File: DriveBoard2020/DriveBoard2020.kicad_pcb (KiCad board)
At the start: 2 copper layers, 57 parts, among them SW0 SW_SPST, SW1 SW_Push, SW2 SW_Push, SW3 SW_Push, SW4 SW_Push, SW5 SW_Push, SW6 SW_Push, U1 MAX232, U2 MAX232, U3 OKI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

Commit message: worked really hard on making layout pretty
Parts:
- moved C6 4.10 mm to (92.3, 49.5)
- moved Conn1 0.13 mm to (105.3, 70.4)
- turned C2 to 270 degrees
- turned C7 to 270 degrees
- turned D10 to 270 degrees
- turned D11 to 270 degrees
- turned D12 to 270 degrees
- turned D13 to 270 degrees
- turned D14 to 270 degrees
- turned D6 to 90 degrees
- turned D8 to 270 degrees
- turned D9 to 270 degrees
- turned R10 to 270 degrees
- turned R12 to 270 degrees
- turned R13 to 270 degrees
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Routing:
- net Tx3: track 158.1 -> 62.5 mm
- net GND: track 94.3 -> 0.00 mm, vias 6 -> 0
- net Tx4: track 111.0 -> 158.3 mm, vias 3 -> 4
- net FR_Motor: track 46.7 -> 10.6 mm, vias 1 -> 0
- net MR_Motor: track 45.5 -> 10.6 mm, vias 1 -> 0
- net +5V: track 90.5 -> 56.2 mm
- net ML_Motor: track 32.8 -> 10.6 mm, vias 1 -> 0
- net switch_direction: track 21.0 -> 0.00 mm, vias 2 -> 0
- net Rx4: track 75.3 -> 88.8 mm, vias 2 -> 4
- net R5_In: track 12.4 -> 0.00 mm
- net Rx6: track 80.1 -> 91.5 mm, vias 2 -> 4
- net Rx3: track 102.1 -> 90.9 mm, vias 0 -> 1
- net RL_Motor: track 40.0 -> 48.7 mm
- net RR_Motor: track 45.4 -> 53.6 mm, vias 1 -> 2
- net R4_In: track 27.6 -> 35.1 mm
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
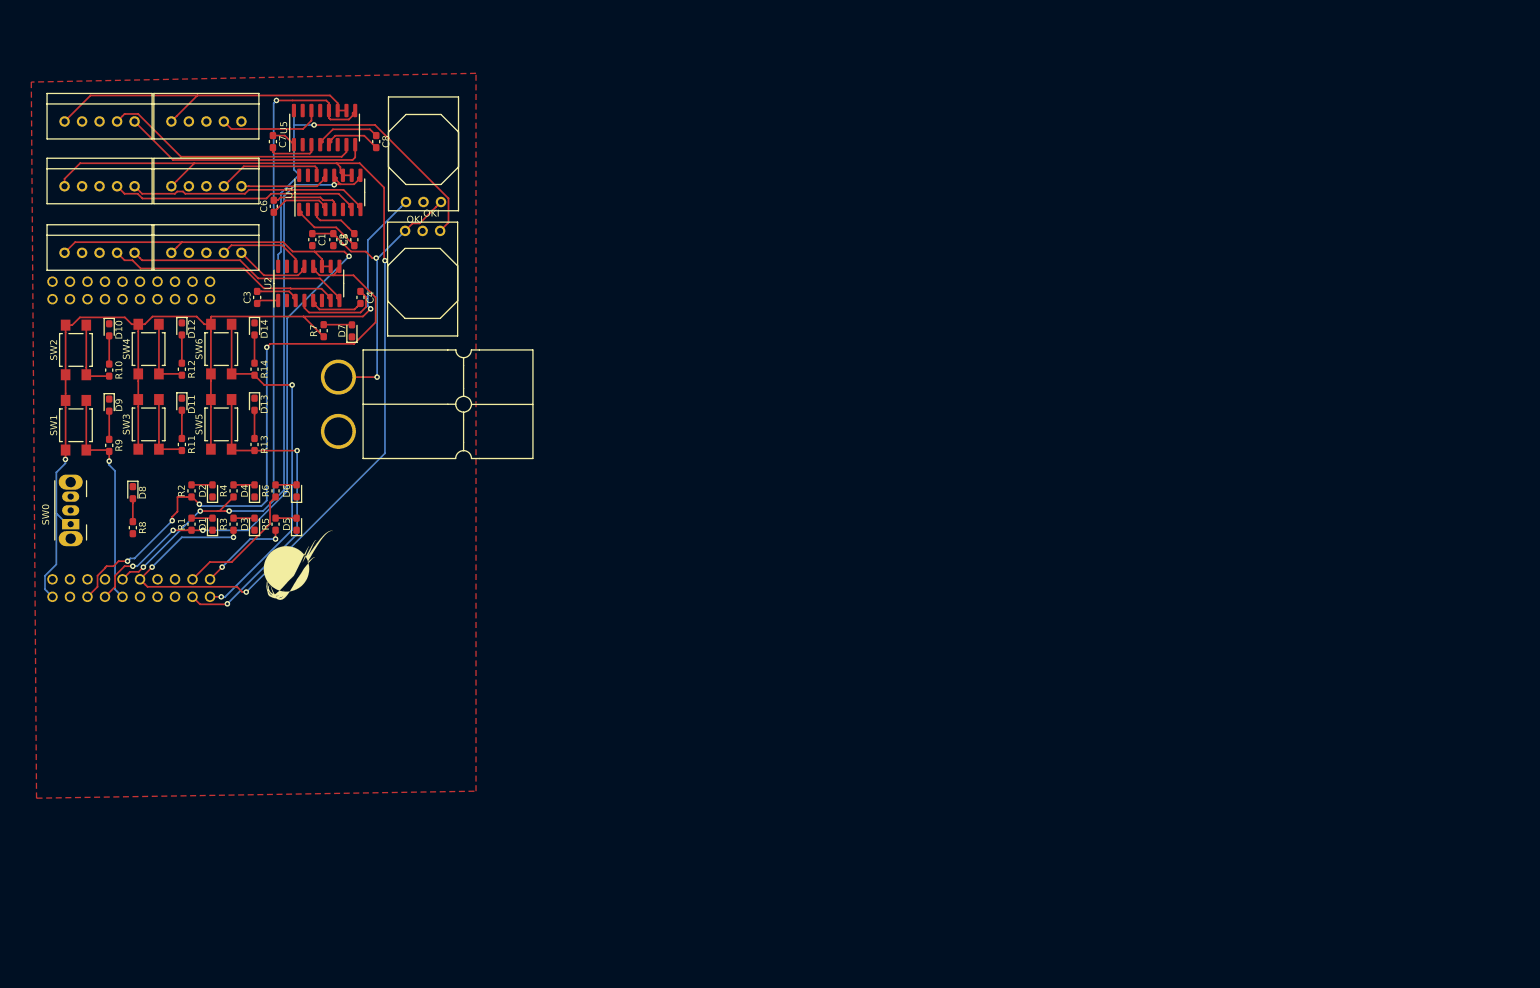
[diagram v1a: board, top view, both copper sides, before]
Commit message: changed and wired 3232's
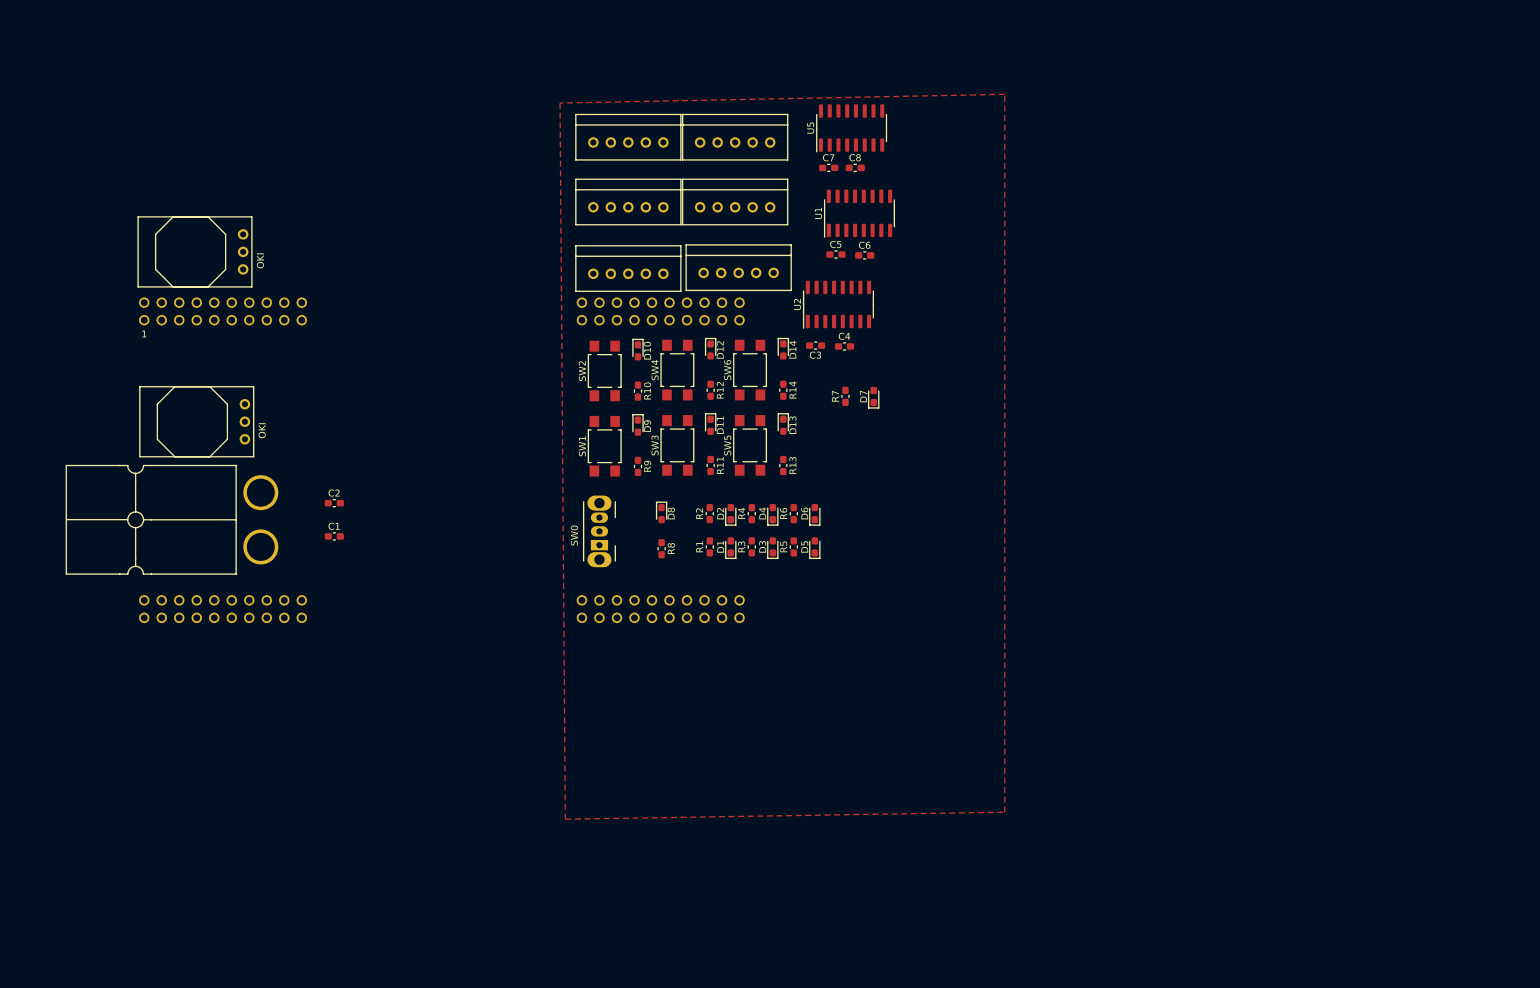
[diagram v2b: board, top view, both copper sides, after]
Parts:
- removed G***: LOGO, MRDT_Silkscreens:0_MRDT_Logo_10mm
- U1, U2, U5: value MAX232 -> MAX_3232
- U4: footprint MRDT_Shields:TM4C129E_Launchpad_X7_THT_BOTTOM -> MRDT_Shields:TM4C129E_Launchpad_FULL_THT_BOTTOM
- moved C6 86.0 mm to (178.1, 56.6), turned to 0 degrees
- moved C3 81.3 mm to (170.9, 69.7), turned to 180 degrees
- moved C7 80.7 mm to (172.8, 43.9), turned to 0 degrees
- moved Conn2 77.3 mm to (159.8, 59.2)
- moved U1 76.9 mm to (177.3, 50.5)
- moved U2 76.9 mm to (174.2, 63.8)
- moved Conn3 76.8 mm to (159.3, 49.7)
- moved Conn4 76.8 mm to (159.3, 40.3)
- moved Conn5 76.8 mm to (143.8, 59.3)
- moved Conn6 76.8 mm to (143.8, 49.7)
- moved Conn7 76.8 mm to (143.8, 40.3)
- moved D10 76.8 mm to (145.2, 70.5)
- moved D11 76.8 mm to (155.7, 81.3)
- moved D12 76.8 mm to (155.7, 70.4)
- moved D13 76.8 mm to (166.2, 81.3)
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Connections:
- Conn3 pad 4: T3_Out -> T2_Out
- Conn3 pad 5: R3_In -> R2_In
- Conn4 pad 4: T5_Out -> T3_Out
- Conn4 pad 5: R5_In -> R3_In
- Conn5 pad 4: T2_Out -> T1_Out
- Conn5 pad 5: R2_In -> R1_In
- Conn6 pad 4: T4_Out -> T2_Out
- Conn6 pad 5: R4_In -> R2_In
- Conn7 pad 4: T6_Out -> T3_Out
- Conn7 pad 5: R6_In -> R3_In
- U1 pad 10: Tx4 -> Net-(U1-Pad10)
- U1 pad 13: R3_In -> R2_In
- U1 pad 14: T3_Out -> T2_Out
- U1 pad 7: T4_Out -> Net-(U1-Pad7)
- U1 pad 8: R4_In -> Net-(U1-Pad8)
- U1 pad 9: Rx4 -> Net-(U1-Pad9)
- U2 pad 1: Net-(C3-Pad1) -> Net-(C3-Pad2)
- U2 pad 10: Tx6 -> Net-(U2-Pad10)
- U2 pad 3: Net-(C3-Pad2) -> Net-(C3-Pad1)
- U2 pad 7: T2_Out -> Net-(U2-Pad7)
- U2 pad 8: R2_In -> Net-(U2-Pad8)
- U2 pad 9: Rx6 -> Net-(U2-Pad9)
- U5 pad 10: Tx3 -> Net-(U5-Pad10)
- U5 pad 13: R5_In -> R3_In
- U5 pad 14: T5_Out -> T3_Out
- U5 pad 7: T6_Out -> Net-(U5-Pad7)
- U5 pad 8: R6_In -> Net-(U5-Pad8)
- U5 pad 9: Rx3 -> Net-(U5-Pad9)
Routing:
- net Tx4: track 158.3 -> 0.00 mm, vias 4 -> 0
- net +3V3: track 149.8 -> 0.00 mm, vias 2 -> 0
- net Tx6: track 120.3 -> 0.00 mm, vias 4 -> 0
- net Rx6: track 91.5 -> 0.00 mm, vias 4 -> 0
- net Rx3: track 90.9 -> 0.00 mm, vias 1 -> 0
- net Rx4: track 88.8 -> 0.00 mm, vias 4 -> 0
- net Tx3: track 62.5 -> 0.00 mm, vias 2 -> 0
- net +5V: track 56.2 -> 0.00 mm, vias 1 -> 0
- net RR_Motor: track 53.6 -> 0.00 mm, vias 2 -> 0
- net RL_Motor: track 48.7 -> 0.00 mm, vias 2 -> 0
- net +12V: track 46.4 -> 0.00 mm, vias 2 -> 0
- net T6_Out: track 37.6 -> 0.00 mm
- net R6_In: track 36.3 -> 0.00 mm
- net T4_Out: track 36.2 -> 0.00 mm
- net R4_In: track 35.1 -> 0.00 mm
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
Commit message: created netlist, began layout
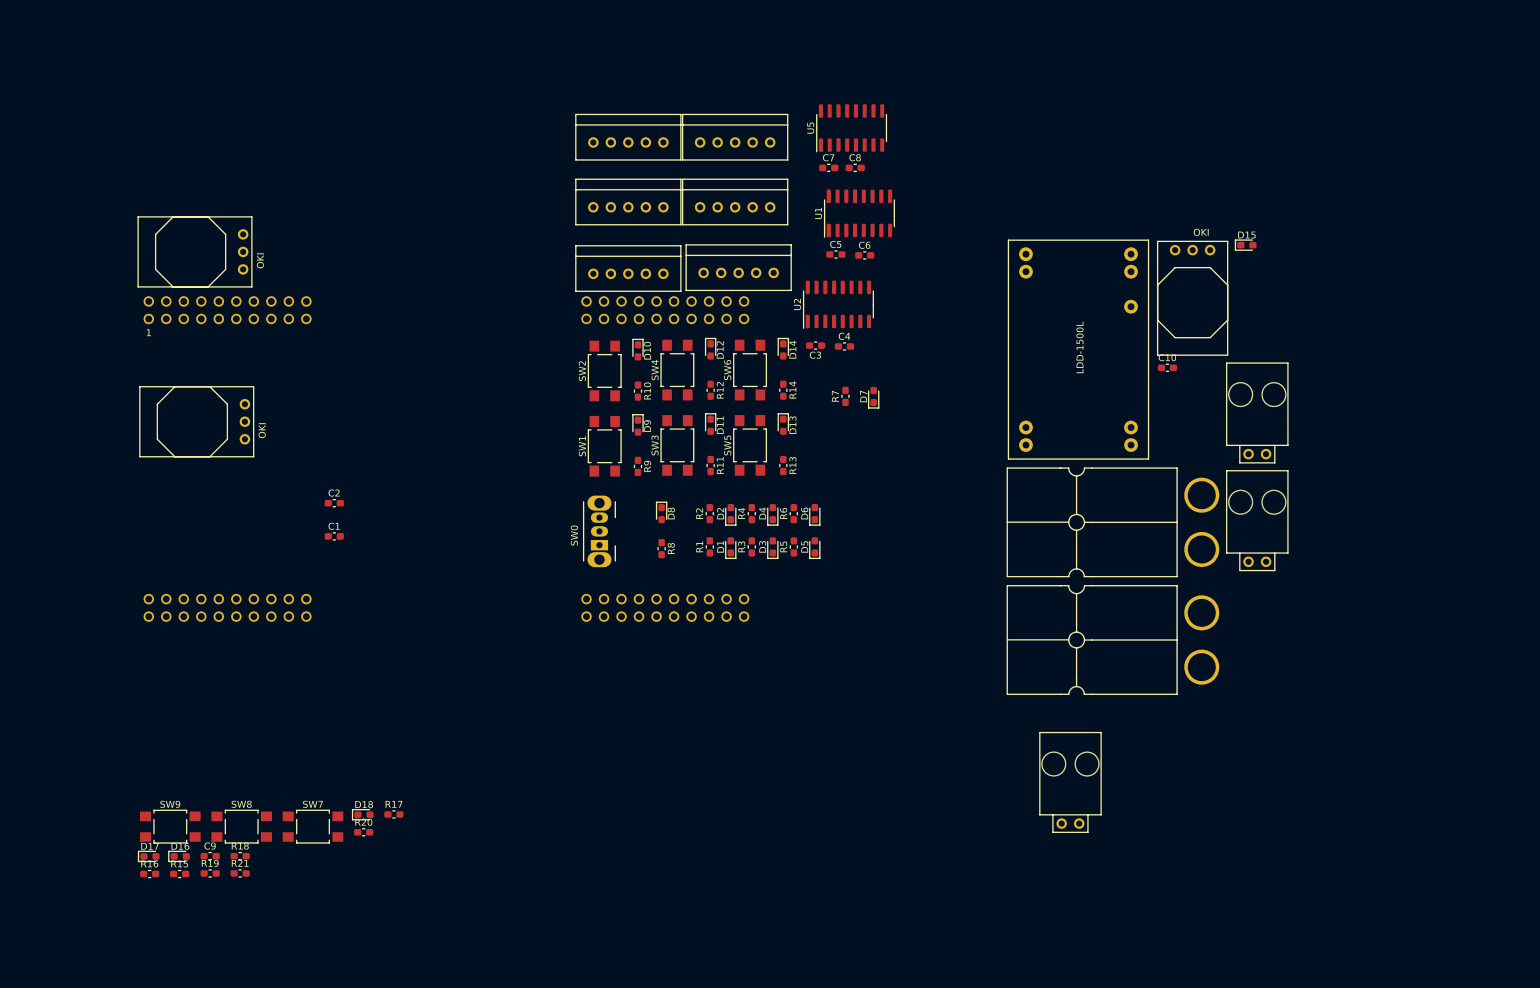
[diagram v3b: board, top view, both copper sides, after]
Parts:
- added C10: 10uF, Capacitor_SMD:C_0603_1608Metric_Pad1.05x0.95mm_HandSolder, F.Cu at (222.0, 72.9)
- added C9: 10uF, Capacitor_SMD:C_0603_1608Metric_Pad1.05x0.95mm_HandSolder, F.Cu at (83.1, 143.8)
- added Conn10: Molex_SL_02, MRDT_Connectors:MOLEX_SL_02_Horizontal, F.Cu at (207.9, 139.1)
- added Conn11: Molex_SL_02, MRDT_Connectors:MOLEX_SL_02_Horizontal, F.Cu at (235.0, 101.1)
- added Conn8: AndersonPP, MRDT_Connectors:Anderson_2_Horizontal_Side_by_Side, F.Cu at (223.4, 120.3)
- added Conn9: Molex_SL_02, MRDT_Connectors:MOLEX_SL_02_Horizontal, F.Cu at (235.0, 85.5)
- added D15: G_LED, LED_SMD:LED_0603_1608Metric_Pad1.05x0.95mm_HandSolder, F.Cu at (233.5, 55.2)
- added D16: G_LED, LED_SMD:LED_0603_1608Metric_Pad1.05x0.95mm_HandSolder, F.Cu at (78.8, 143.8)
- added D17: Org_LED, LED_SMD:LED_0603_1608Metric_Pad1.05x0.95mm_HandSolder, F.Cu at (74.4, 143.8)
- added D18: Org_LED, LED_SMD:LED_0603_1608Metric_Pad1.05x0.95mm_HandSolder, F.Cu at (105.4, 137.8)
- added R15: 10K, Resistor_SMD:R_0603_1608Metric_Pad1.05x0.95mm_HandSolder, F.Cu at (78.7, 146.4)
- added R16: 10K, Resistor_SMD:R_0603_1608Metric_Pad1.05x0.95mm_HandSolder, F.Cu at (74.3, 146.4)
- added R17: 10K, Resistor_SMD:R_0603_1608Metric_Pad1.05x0.95mm_HandSolder, F.Cu at (109.8, 137.7)
- added R18: 500, Resistor_SMD:R_0603_1608Metric_Pad1.05x0.95mm_HandSolder, F.Cu at (87.4, 143.8)
- added R19: 500, Resistor_SMD:R_0603_1608Metric_Pad1.05x0.95mm_HandSolder, F.Cu at (83.1, 146.3)
- added R20: 500, Resistor_SMD:R_0603_1608Metric_Pad1.05x0.95mm_HandSolder, F.Cu at (105.4, 140.3)
- added R21: 500, Resistor_SMD:R_0603_1608Metric_Pad1.05x0.95mm_HandSolder, F.Cu at (87.4, 146.3)
- added SW7: SW_Push, Button_Switch_SMD:SW_SPST_TL3305A, F.Cu at (98.0, 139.5)
- added SW8: SW_Push, Button_Switch_SMD:SW_SPST_TL3305A, F.Cu at (87.7, 139.5)
- added SW9: SW_Push, Button_Switch_SMD:SW_SPST_TL3305A, F.Cu at (77.3, 139.5)
- added U7: OKI, MRDT_Devices:OKI_Horizontal, F.Cu at (220.5, 54.6)
- added U8: LDD-1500L, MRDT_Devices:LDD-1500L_LED_DRIVER, F.Cu at (198.9, 86.2)
- moved Conn1 136.5 mm to (223.4, 103.2)
- moved U4 0.68 mm to (72.9, 110.3)
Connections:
- U4 pad +3V3`: +3V3 -> (no net)
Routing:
- removed copper zone on F.Cu, net GND

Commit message: minor changes to layout
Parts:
- moved Conn8 136.9 mm to (87.6, 102.9)
- moved Conn1 136.7 mm to (87.6, 86.9)
- moved R14 116.8 mm to (267.0, 135.4)
- moved D14 116.8 mm to (267.0, 129.5)
- moved SW6 116.8 mm to (262.1, 132.5)
- moved D11 116.8 mm to (255.5, 141.9)
- moved D13 116.8 mm to (266.1, 141.9)
- moved R9 116.8 mm to (245.0, 147.8)
- moved SW1 116.8 mm to (240.2, 144.9)
- moved SW3 116.8 mm to (250.7, 144.8)
- moved D9 116.8 mm to (245.0, 142.0)
- moved R11 116.8 mm to (255.5, 147.7)
- moved R13 116.8 mm to (266.1, 147.7)
- moved SW5 116.8 mm to (261.2, 144.8)
- moved D10 116.1 mm to (245.2, 129.4)
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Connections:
- Conn8 pad 2: +12VA -> (no net)
- U4 pad PD4: FL_Motor -> Net-(U4-PadPD4)
- U4 pad PD5: FR_Motor -> Net-(U4-PadPD5)
- U4 pad PN4: RR_Motor -> Net-(U4-PadPN4)
- U4 pad PN5: RL_Motor -> Net-(U4-PadPN5)
- U4 pad PP4: MR_Motor -> Net-(U4-PadPP4)
- U4 pad PQ0: ML_Motor -> Net-(U4-PadPQ0)

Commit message: working on layout
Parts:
- moved D7 184.8 mm to (88.2, 44.6)
- moved R7 184.8 mm to (84.1, 44.6)
- moved D15 129.7 mm to (111.4, 98.9), turned to 90 degrees
- moved D9 129.6 mm to (136.3, 71.5)
- moved R9 129.6 mm to (136.3, 77.3)
- moved SW1 129.6 mm to (131.4, 74.4)
- moved D14 127.2 mm to (165.2, 53.1)
- moved R14 127.2 mm to (165.2, 59.0)
- moved SW6 127.2 mm to (160.4, 56.1)
- moved U7 127.1 mm to (99.6, 93.7)
- moved D13 126.3 mm to (175.9, 53.4)
- moved R13 126.3 mm to (175.9, 59.2)
- moved SW5 126.3 mm to (171.1, 56.3)
- moved D11 119.0 mm to (159.6, 71.5)
- moved SW3 119.0 mm to (154.7, 74.4)
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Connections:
- U4 pad +3V3: (no net) -> Net-(U4-Pad+3V3)
- U4 pad +5V: (no net) -> Net-(U4-Pad+5V)
- U4 pad PA6: (no net) -> Net-(U4-PadPA6)
- U4 pad PA7: (no net) -> Headlight_OnOff_PWM
- U4 pad PB2: (no net) -> Net-(U4-PadPB2)
- U4 pad PB3: (no net) -> Net-(U4-PadPB3)
- U4 pad PC4: (no net) -> Net-(U4-PadPC4)
- U4 pad PC5: (no net) -> Net-(U4-PadPC5)
- U4 pad PC6: (no net) -> Net-(U4-PadPC6)
- U4 pad PC7: (no net) -> Net-(U4-PadPC7)
- U4 pad PD0: (no net) -> Net-(U4-PadPD0)
- U4 pad PD1: (no net) -> Net-(U4-PadPD1)
- U4 pad PD3: (no net) -> Net-(U4-PadPD3)
- U4 pad PD7: (no net) -> Net-(U4-PadPD7)
- U4 pad PE0: (no net) -> Net-(U4-PadPE0)
- U4 pad PE1: (no net) -> Net-(U4-PadPE1)
- U4 pad PE2: (no net) -> Net-(U4-PadPE2)
- U4 pad PE3: (no net) -> Net-(U4-PadPE3)
- U4 pad PE4: (no net) -> Net-(U4-PadPE4)
- U4 pad PE5: (no net) -> Net-(U4-PadPE5)
- U4 pad PF1: (no net) -> Dout_NeoPixel
- U4 pad PF2: (no net) -> Net-(U4-PadPF2)
- U4 pad PF3: (no net) -> Net-(U4-PadPF3)
- U4 pad PG0: (no net) -> Net-(U4-PadPG0)
- U4 pad PG1: (no net) -> Net-(U4-PadPG1)
- U4 pad PH0: (no net) -> Net-(U4-PadPH0)
- U4 pad PH1: (no net) -> ML_Motor
- U4 pad PH2: (no net) -> Net-(U4-PadPH2)
- U4 pad PH3: (no net) -> Net-(U4-PadPH3)
- U4 pad PK2: switch_direction -> Net-(U4-PadPK2)
- U4 pad PK4: (no net) -> Net-(U4-PadPK4)
- U4 pad PK5: (no net) -> FL_Motor
- U4 pad PK6: (no net) -> MR_Motor
- U4 pad PK7: (no net) -> Net-(U4-PadPK7)
- U4 pad PL0: (no net) -> Net-(U4-PadPL0)
- U4 pad PL1: (no net) -> Net-(U4-PadPL1)
- U4 pad PL2: (no net) -> Net-(U4-PadPL2)
- U4 pad PL3: (no net) -> Net-(U4-PadPL3)
- U4 pad PL4: (no net) -> NeoPixel_White
- U4 pad PL5: (no net) -> NeoPixel_Pattern
- U4 pad PM0: (no net) -> FR_Motor
- U4 pad PM1: (no net) -> Net-(U4-PadPM1)
- U4 pad PM2: (no net) -> Net-(U4-PadPM2)
- U4 pad PM3: (no net) -> Headlight_Power
- U4 pad PM4: (no net) -> Net-(U4-PadPM4)
- U4 pad PM5: (no net) -> Net-(U4-PadPM5)
- U4 pad PM6: (no net) -> switch_direction
- U4 pad PM7: (no net) -> Net-(U4-PadPM7)
- U4 pad PN2: (no net) -> Net-(U4-PadPN2)
- U4 pad PN3: (no net) -> Net-(U4-PadPN3)
- U4 pad PP2: (no net) -> Net-(U4-PadPP2)
- U4 pad PP3: (no net) -> RR_Motor
- U4 pad PP5: (no net) -> Net-(U4-PadPP5)
- U4 pad PQ1: (no net) -> RL_Motor
- U4 pad PQ2: (no net) -> Net-(U4-PadPQ2)
- U4 pad PQ3: (no net) -> Net-(U4-PadPQ3)
- U4 pad Rese: (no net) -> Net-(U4-PadRese)
